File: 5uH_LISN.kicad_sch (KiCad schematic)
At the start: 79 parts, among them J1 Conn_Coaxial, J2 Conn_Coaxial, J3 BANANA_CONN, J4 BANANA_CONN, J5 BANANA_CONN, J6 BANANA_CONN, J7 BANANA_CONN, J8 BANANA_CONN

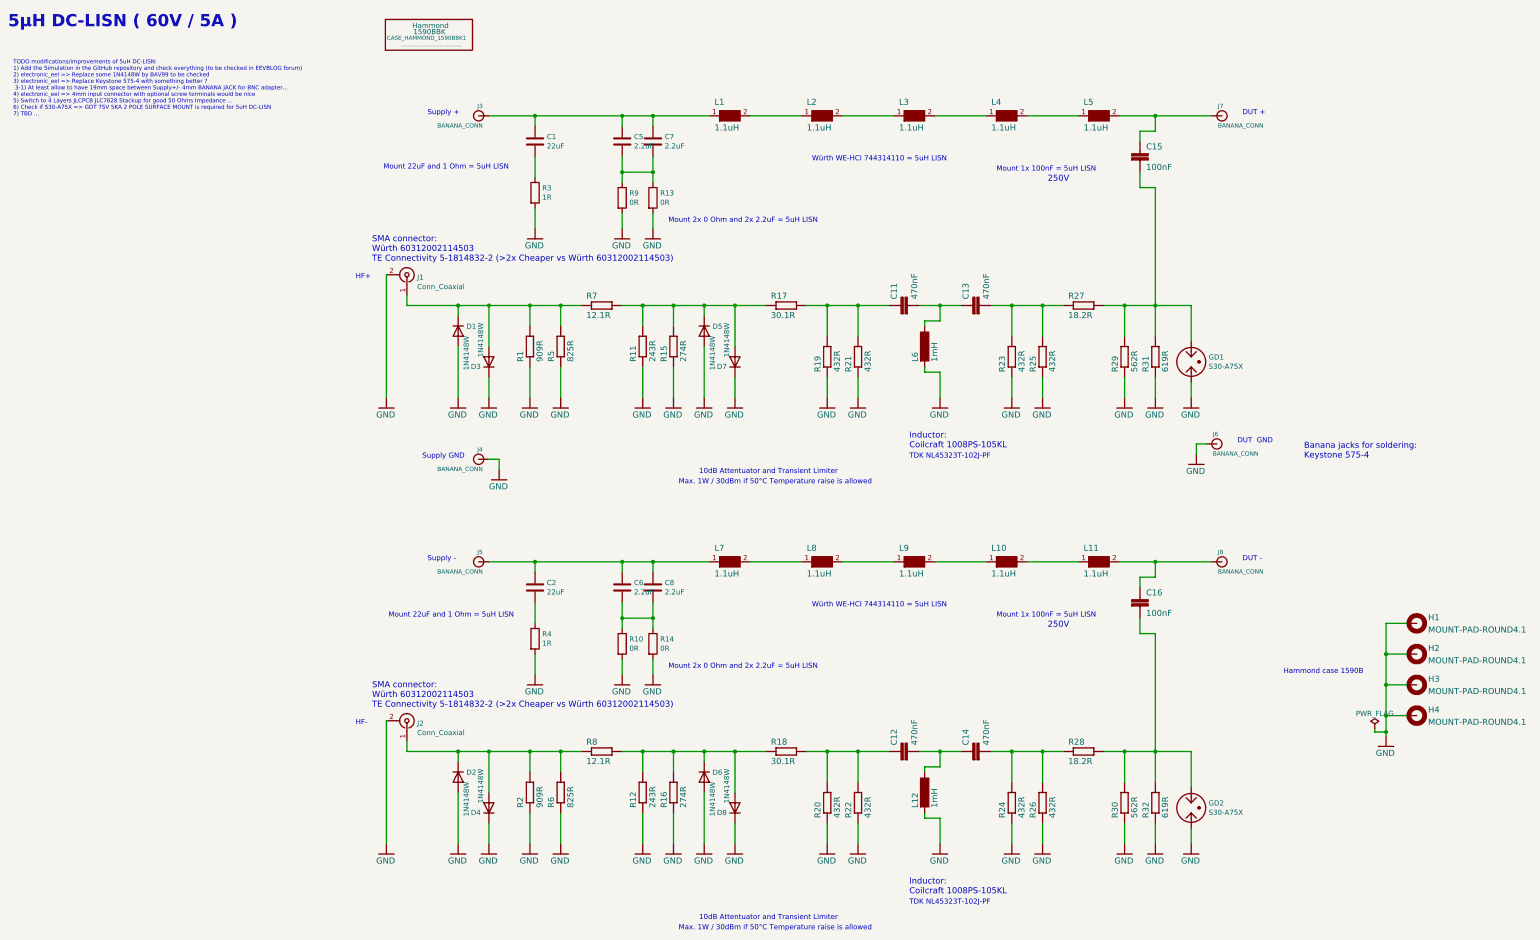
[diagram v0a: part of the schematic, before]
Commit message: LISN V1 R0 * Added simulation with LTSpice of the 10dB Attenuator / Transient Filter (with default 1N4148 and BAV99) * Replaced some 1N4148W by BAV99 from Nexperia (to reach up to 400MHz flat 10dB Attenuator / Transient Filter) * Changed space to have 19.06mm between Supply / DUT "+" <=> "GND" <=> "-" => 4mm BANANA JACK for BNC adapter * Changed Keystone Electronics 575-4 which are too short for banana by Keystone Electronics 575-8
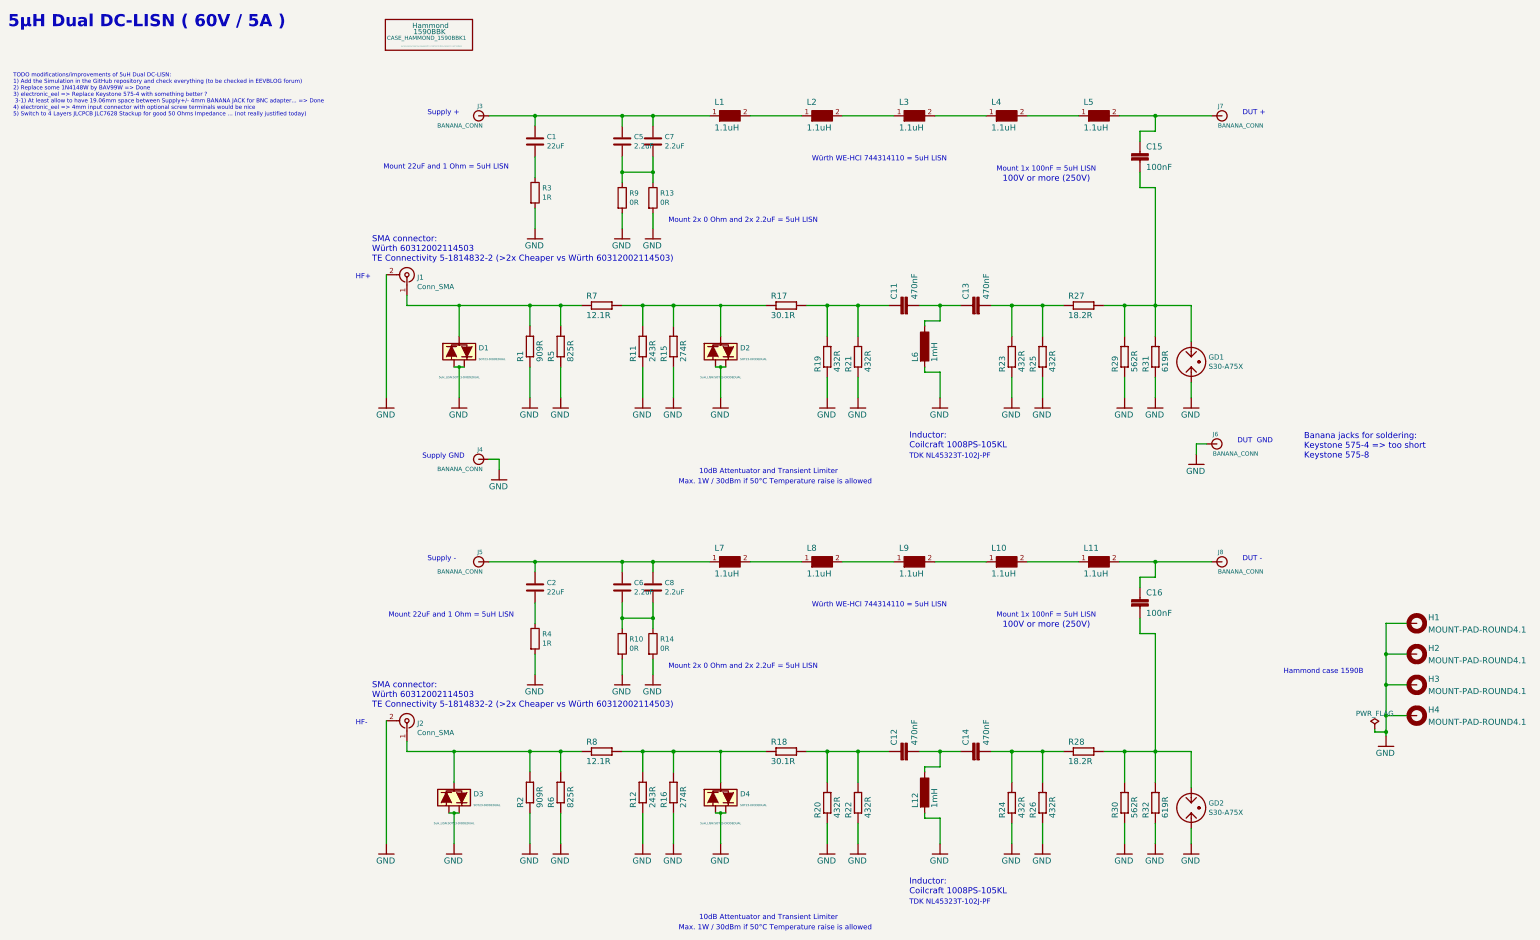
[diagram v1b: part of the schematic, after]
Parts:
- removed D1, D2, D3, D4, D5, D6, D7, D8: 1N4148W, Diode_SMD:D_SOD-123, symbol 5uH_LISN-rescue:D-Device
- added D1, D2, D3, D4: SOT23-DIODEDUAL, 5uH_LISN:SOT23-DIODEDUAL, symbol SOT23-DIODEDUAL:SOT23-DIODEDUAL
- C11, C12, C13, C14: manf# 08051C474K4Z2A -> 08051C474KAT2A
- J1, J2: value Conn_Coaxial -> Conn_SMA
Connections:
- net GND: now also D1.1, D1.2, D2.1, D2.2, D3.1, D3.2, D4.1, D4.2
- net at J1.1 (In), R1.2, R5.2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: now also D1.3
- net at R11.2, R15.2, R17.1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: now also D2.3
- net at J2.1 (In), R2.2, R6.2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: now also D3.3
- net at R12.2, R16.2, R18.1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: now also D4.3
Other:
- note added: "100V or more (250V)"
- note added: "5µH Dual DC-LISN ( 60V / 5A )"
- note added: "Banana jacks for soldering: Keystone 575-4 => too short Keystone 575-8"
- note added: "TODO modifications/improvements of 5uH Dual DC-LISN: 1) Add the Simulation in the GitHub repository and check everything (to be checked in EEVBLOG forum) 2) Replace some 1N4148W by BAV99W => Done 3) electronic_eel => Replace Keystone 575-4 with something better ? 3-1) At least allow to have 19.06mm space between Supply+/- 4mm BANANA JACK for BNC adapter... => Done 4) electronic_eel => 4mm input c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"
- note removed: "250V"
- note removed: "5µH DC-LISN ( 60V / 5A )"
- note removed: "Banana jacks for soldering: Keystone 575-4"
- note removed: "TODO modifications/improvements of 5uH DC-LISN: 1) Add the Simulation in the GitHub repository and check everything (to be checked in EEVBLOG forum) 2) electronic_eel => Replace some 1N4148W by BAV99 to be checked 3) electronic_eel => Replace Keystone 575-4 with something better ? 3-1) At least allow to have 19mm space between Supply+/- 4mm BANANA JACK for BNC adapter... 4) electronic_eel => 4mm 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"
- company: F.Siebel -> F.Siebel / B.VERNOUX
